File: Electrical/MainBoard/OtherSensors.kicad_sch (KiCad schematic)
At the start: 23 parts, among them J10 Refl_Mount, J11 Refl_Mount, J12 Refl_PCB_Connect, J13 Refl_PCB_Connect, J14 Refl_PCB_Connect, J9 Refl_Mount, K1 QRE1113GR, K2 QRE1113GR, K3 QRE1113GR, SW4 SW_SPST, SW5 SW_SPST, SW6 SW_SPST, SW7 SW_SPST

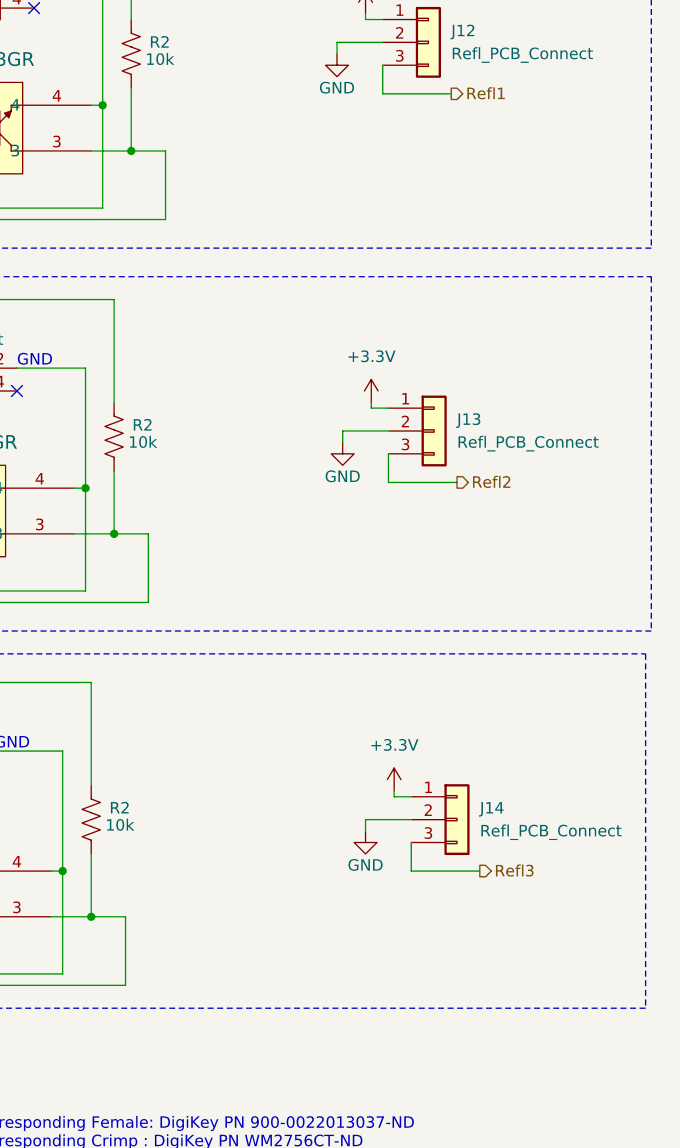
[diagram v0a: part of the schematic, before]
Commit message: Add more schematics and begin floorplanning
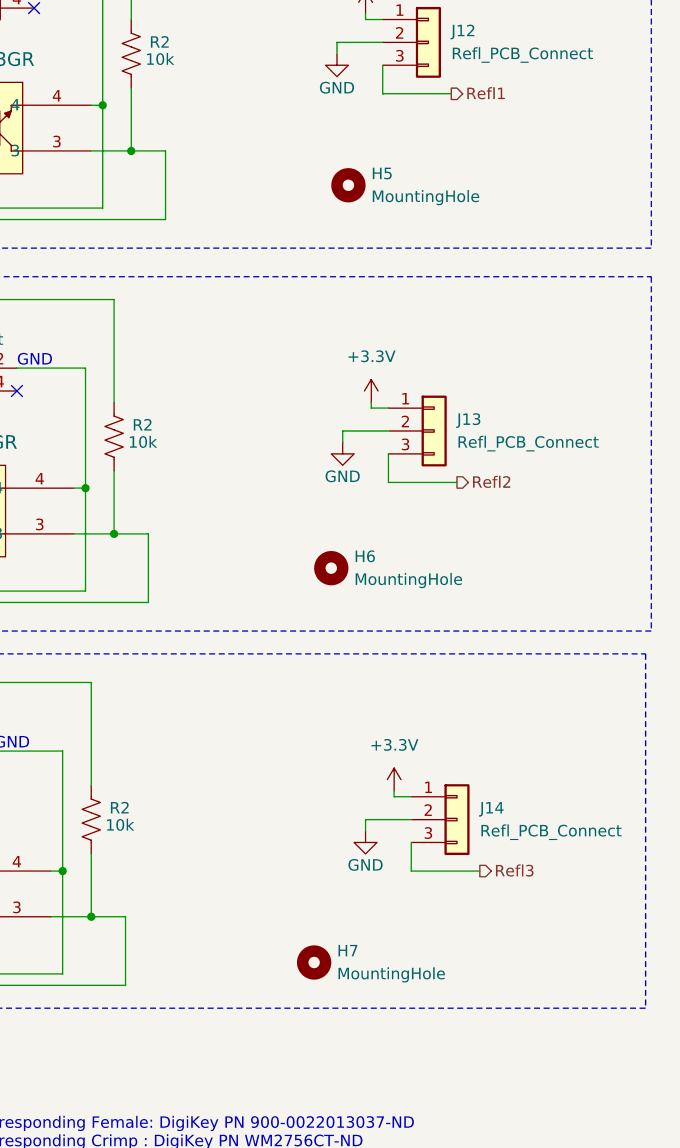
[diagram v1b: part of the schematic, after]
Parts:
- added H5, H6, H7: MountingHole, MountingHole:MountingHole_2.2mm_M2, symbol Mechanical:MountingHole

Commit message: Begin layout of pcb
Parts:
- renumbered H7 to H5, H5 to H7, J11 to J10, J10 to J11, J9 to J12, J12 to J13, J13 to J14, J14 to J15, K3 to K1, K1 to K3, SW7 to SW10, SW4 to SW7, SW5 to SW8, SW6 to SW9
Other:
- moved on the sheet: R2

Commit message: Some finishing touches to the board
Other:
- note added: "Corresponding Female: DigiKey PN 900-0022013037-ND Corresponding Crimp : DigiKey PN WM2756CT-ND"
- note removed: "Corresponding Female: DigiKey PN 900-0022013037-ND Corresponding Crimp : DigiKey PN WM2756CT-ND Button : DigiKey PN EG2025-ND"
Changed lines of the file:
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@@
     (effects (font (size 1.27 1.27)) (justify left bottom))
   )
-  (text "Corresponding Female: DigiKey PN 900-0022013037-ND\nCorresponding Crimp : DigiKey PN WM2756CT-ND\nButton          	: DigiKey PN EG2025-ND"
+  (text "Corresponding Female: DigiKey PN 900-0022013037-ND\nCorresponding Crimp : DigiKey PN WM2756CT-ND\n"
     (at 290.83 203.2 0)
     (effects (font (size 1.27 1.27)) (justify left bottom))

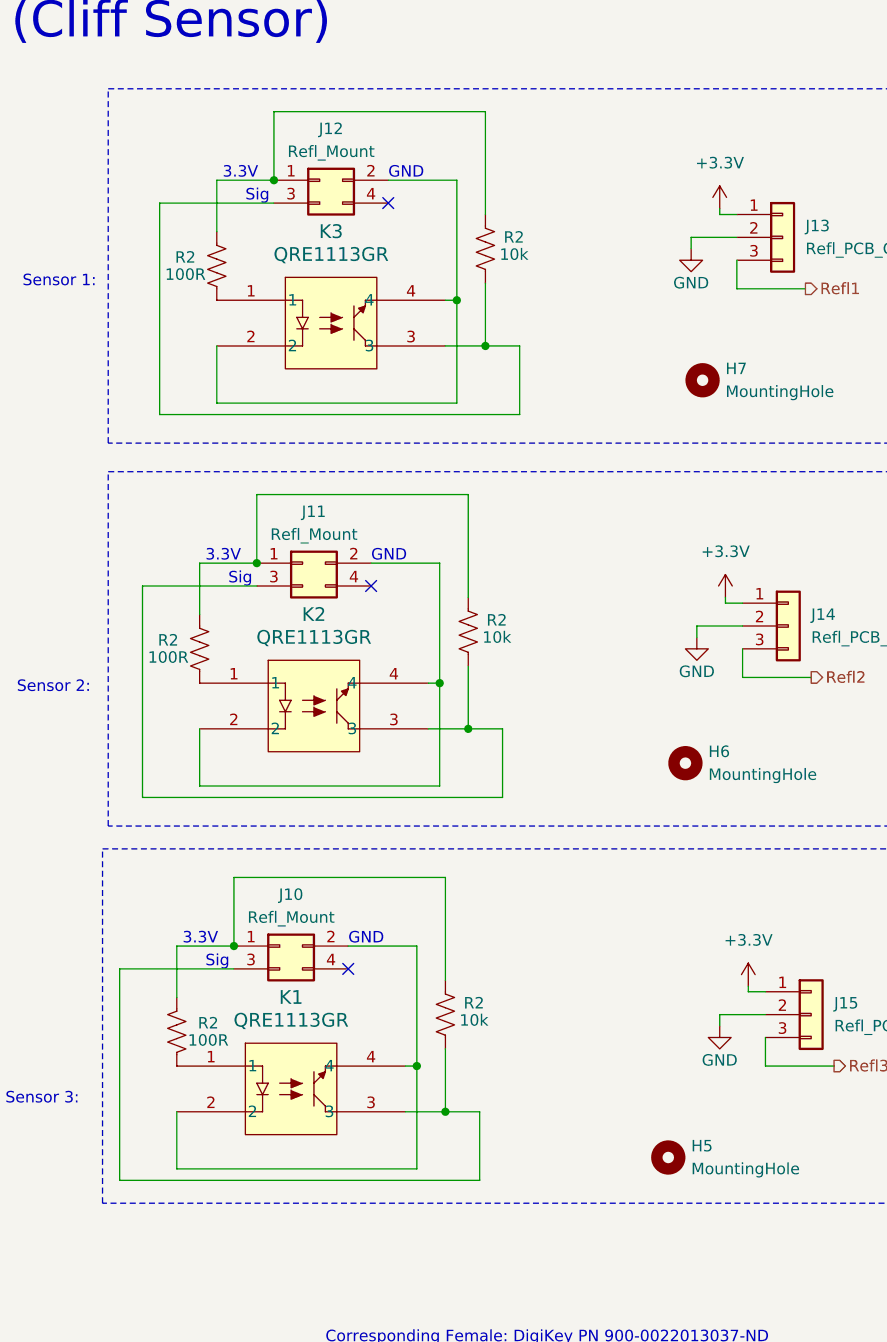
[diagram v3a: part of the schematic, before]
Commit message: Move reflectlive sensors to own schematic
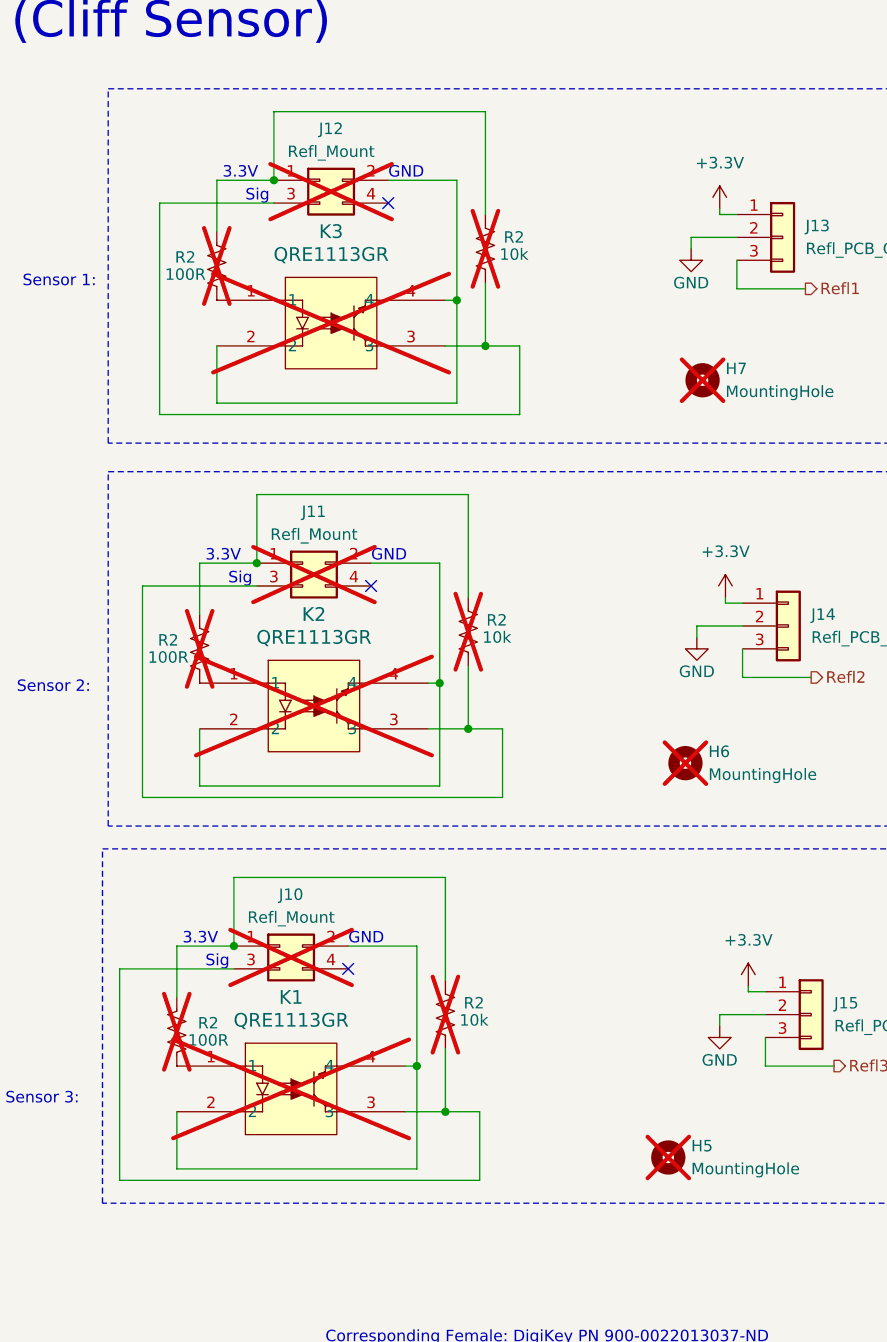
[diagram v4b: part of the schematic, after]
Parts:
- H5, H6, H7, J10, J11, J12, K1, K2, K3, R2: now not fitted; now left out of the parts list
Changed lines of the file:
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@@
   )
   (symbol (lib_id "Connector_Generic:Conn_02x02_Odd_Even") (at 285.75 156.845 0) (unit 1)
-    (in_bom yes) (on_board yes) (dnp no) (fields_autoplaced)
+    (in_bom no) (on_board no) (dnp yes) (fields_autoplaced)
     (property "Reference" "J10" (at 287.02 151.13 0)
       (effects (font (size 1.27 1.27)))
@@
   )
   (symbol (lib_id "Device:R_US") (at 306.705 121.92 180) (unit 1)
-    (in_bom yes) (on_board yes) (dnp no)
+    (in_bom no) (on_board no) (dnp yes)
     (property "Reference" "R2" (at 309.88 120.65 0)
       (effects (font (size 1.27 1.27)))
@@
   )
   (symbol (lib_id "Connector_Generic:Conn_02x02_Odd_Even") (at 290.195 71.755 0) (unit 1)
-    (in_bom yes) (on_board yes) (dnp no) (fields_autoplaced)
+    (in_bom no) (on_board no) (dnp yes) (fields_autoplaced)
     (property "Reference" "J12" (at 291.465 66.04 0)
       (effects (font (size 1.27 1.27)))
@@
   )
   (symbol (lib_id "Device:R_US") (at 278.765 81.28 180) (unit 1)
-    (in_bom yes) (on_board yes) (dnp no)
+    (in_bom no) (on_board no) (dnp yes)
     (property "Reference" "R2" (at 275.2725 80.3275 0)
       (effects (font (size 1.27 1.27)))
@@
   )
   (symbol (lib_id "Device:R_US") (at 274.32 166.37 0) (mirror x) (unit 1)
-    (in_bom yes) (on_board yes) (dnp no)
+    (in_bom no) (on_board no) (dnp yes)
     (property "Reference" "R2" (at 277.8125 165.4175 0)
       (effects (font (size 1.27 1.27)))
@@
   )
   (symbol (lib_id "RobotLibary:QRE1113GR") (at 278.765 85.09 0) (unit 1)
-    (in_bom yes) (on_board yes) (dnp no) (fields_autoplaced)
+    (in_bom no) (on_board no) (dnp yes) (fields_autoplaced)
     (property "Reference" "K3" (at 291.465 77.47 0)
       (effects (font (size 1.524 1.524)))
@@
   )
   (symbol (lib_id "Mechanical:MountingHole") (at 328.93 180.34 0) (unit 1)
-    (in_bom yes) (on_board yes) (dnp no) (fields_autoplaced)
+    (in_bom no) (on_board no) (dnp yes) (fields_autoplaced)
     (property "Reference" "H5" (at 331.47 179.07 0)
       (effects (font (size 1.27 1.27)) (justify left))
@@
   )
   (symbol (lib_id "Device:R_US") (at 304.165 164.465 180) (unit 1)
-    (in_bom yes) (on_board yes) (dnp no)
+    (in_bom no) (on_board no) (dnp yes)
     (property "Reference" "R2" (at 307.34 163.195 0)
       (effects (font (size 1.27 1.27)))
@@
   )
   (symbol (lib_id "Mechanical:MountingHole") (at 332.74 93.98 0) (unit 1)
-    (in_bom yes) (on_board yes) (dnp no) (fields_autoplaced)
+    (in_bom no) (on_board no) (dnp yes) (fields_autoplaced)
     (property "Reference" "H7" (at 335.28 92.71 0)
       (effects (font (size 1.27 1.27)) (justify left))
@@
   )
   (symbol (lib_id "Connector_Generic:Conn_02x02_Odd_Even") (at 288.29 114.3 0) (unit 1)
-    (in_bom yes) (on_board yes) (dnp no) (fields_autoplaced)
+    (in_bom no) (on_board no) (dnp yes) (fields_autoplaced)
     (property "Reference" "J11" (at 289.56 108.585 0)
       (effects (font (size 1.27 1.27)))
@@
   )
   (symbol (lib_id "RobotLibary:QRE1113GR") (at 274.32 170.18 0) (unit 1)
-    (in_bom yes) (on_board yes) (dnp no) (fields_autoplaced)
+    (in_bom no) (on_board no) (dnp yes) (fields_autoplaced)
     (property "Reference" "K1" (at 287.02 162.56 0)
       (effects (font (size 1.524 1.524)))
@@
   )
   (symbol (lib_id "Mechanical:MountingHole") (at 330.835 136.525 0) (unit 1)
-    (in_bom yes) (on_board yes) (dnp no) (fields_autoplaced)
+    (in_bom no) (on_board no) (dnp yes) (fields_autoplaced)
     (property "Reference" "H6" (at 333.375 135.255 0)
       (effects (font (size 1.27 1.27)) (justify left))
@@
   )
   (symbol (lib_id "Device:R_US") (at 308.61 79.375 180) (unit 1)
-    (in_bom yes) (on_board yes) (dnp no)
+    (in_bom no) (on_board no) (dnp yes)
     (property "Reference" "R2" (at 311.785 78.105 0)
       (effects (font (size 1.27 1.27)))
@@
   )
   (symbol (lib_id "Device:R_US") (at 276.86 123.825 180) (unit 1)
-    (in_bom yes) (on_board yes) (dnp no)
+    (in_bom no) (on_board no) (dnp yes)
     (property "Reference" "R2" (at 273.3675 122.8725 0)
       (effects (font (size 1.27 1.27)))
@@
   )
   (symbol (lib_id "RobotLibary:QRE1113GR") (at 276.86 127.635 0) (unit 1)
-    (in_bom yes) (on_board yes) (dnp no) (fields_autoplaced)
+    (in_bom no) (on_board no) (dnp yes) (fields_autoplaced)
     (property "Reference" "K2" (at 289.56 120.015 0)
       (effects (font (size 1.524 1.524)))

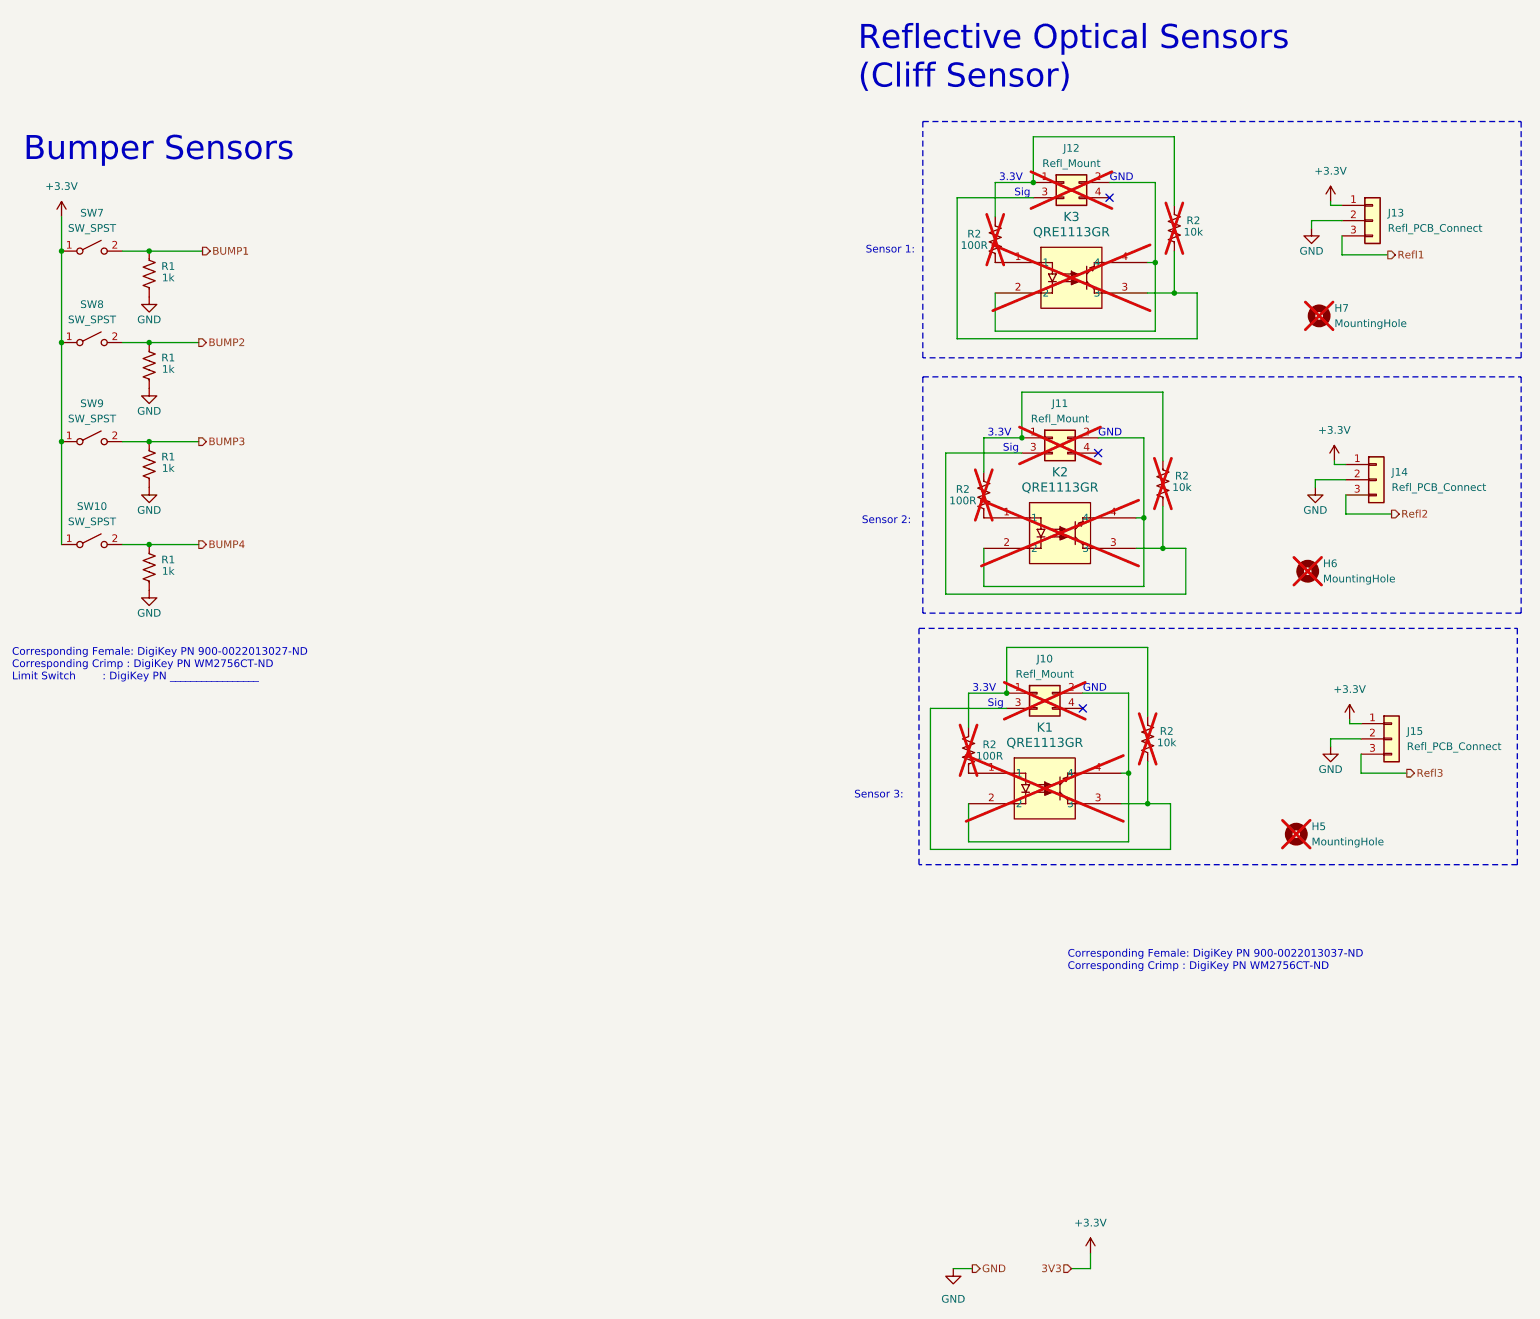
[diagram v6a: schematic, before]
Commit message: Fix SPI3 and make visual improvements
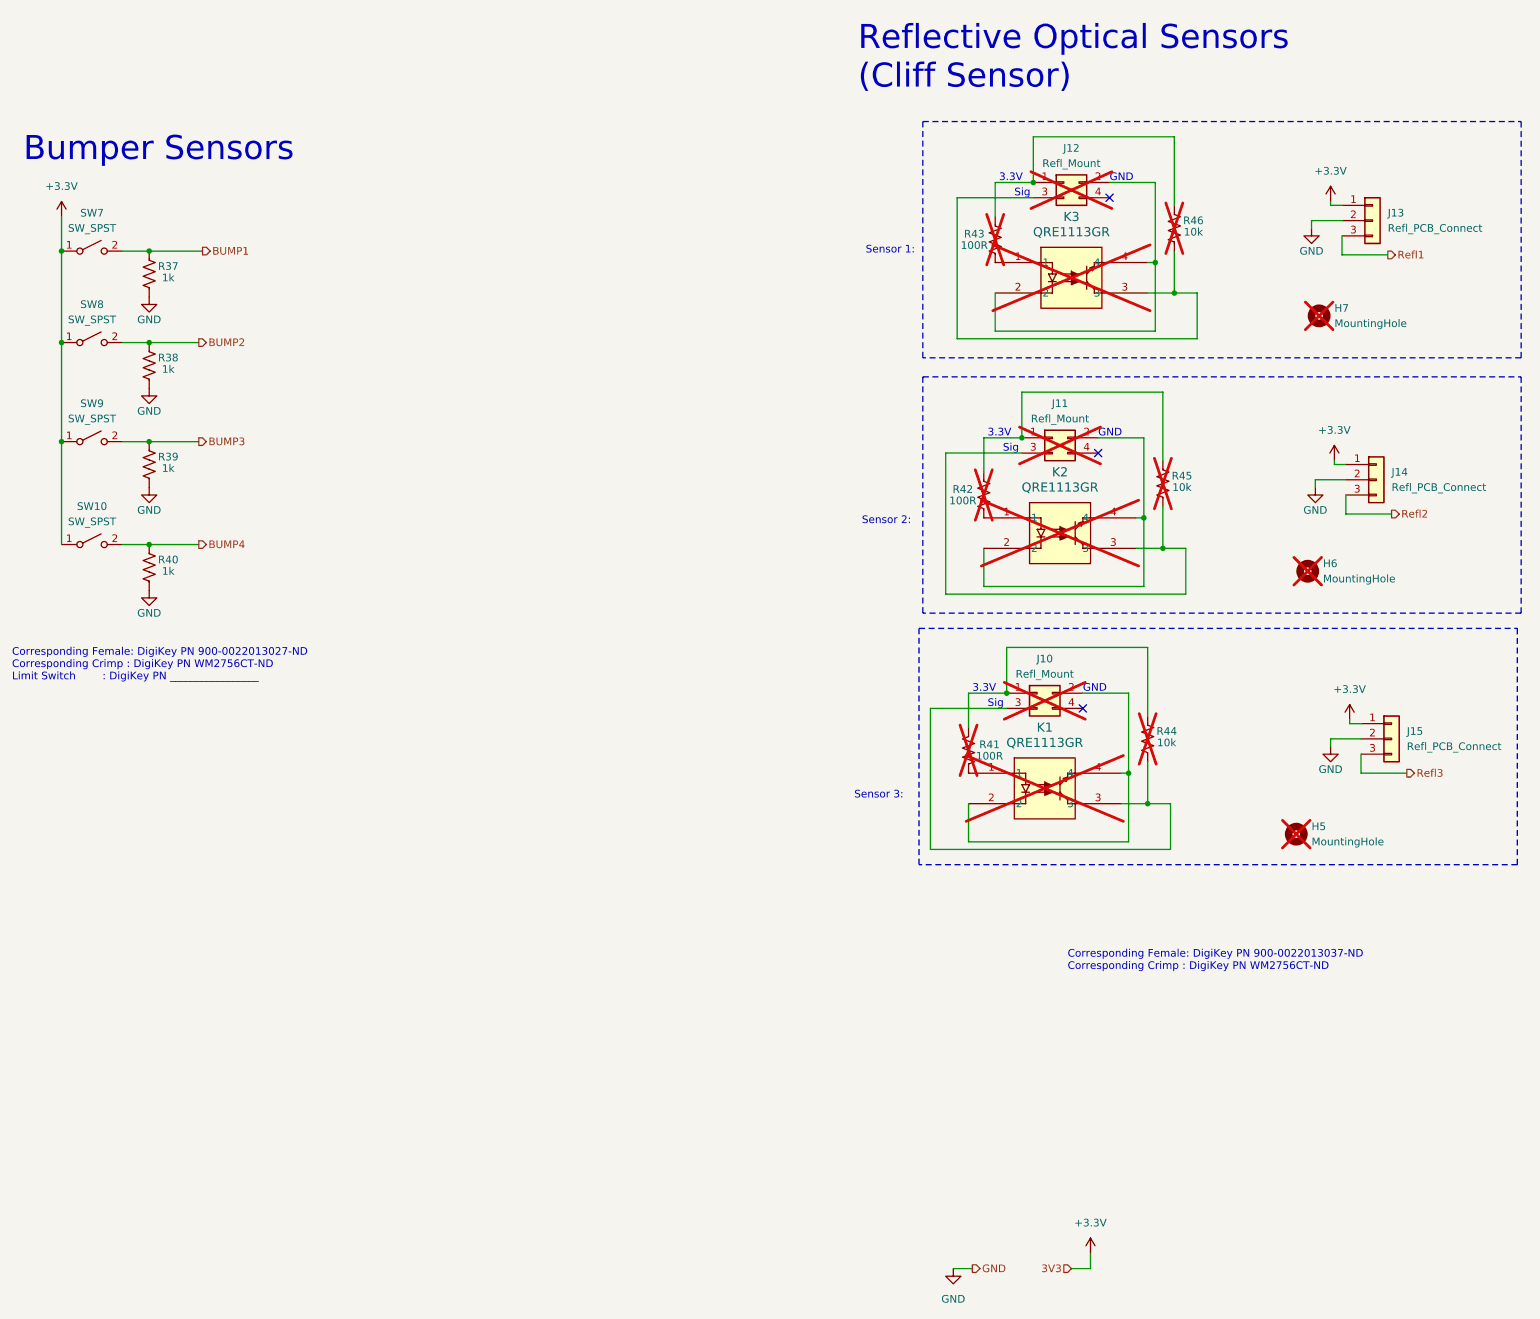
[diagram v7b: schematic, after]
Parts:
- renumbered R1 to R37, R1 to R38, R1 to R39, R1 to R40, R2 to R41, R2 to R42, R2 to R43, R2 to R44, R2 to R45, R2 to R46
